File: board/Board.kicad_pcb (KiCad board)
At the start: 2 copper layers, 58.5 x 58.5 mm, 71 parts, among them J14 CONN_01X02, J15 CONN_01X07, J16 GS2, SW1 SW_Push, U1 STM32F410RBTx, U2 SN74LVC1G04, U3 LF33ABDT-TR, U4 ICM-20689, U5 MAG3110, U6 MS5637, Y1 25 MHz

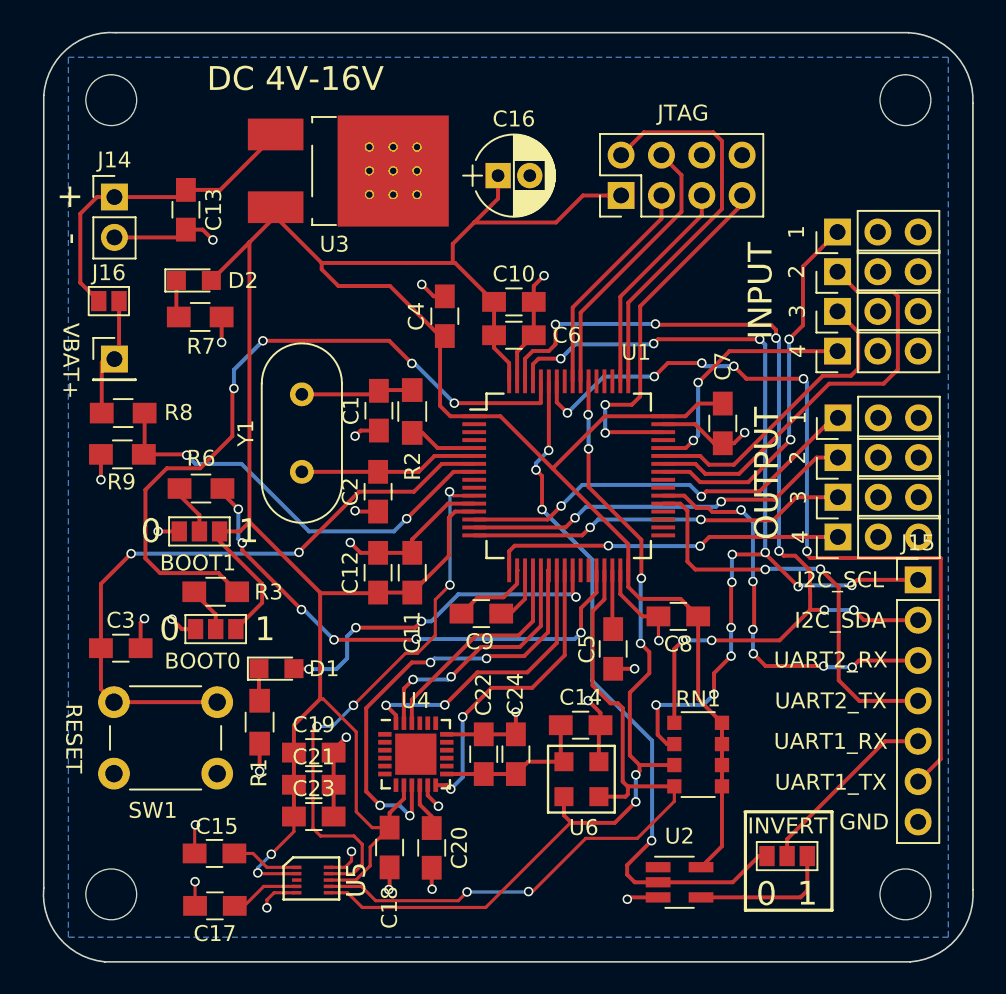
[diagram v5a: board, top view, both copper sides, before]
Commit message: fixed a few unconnected pads
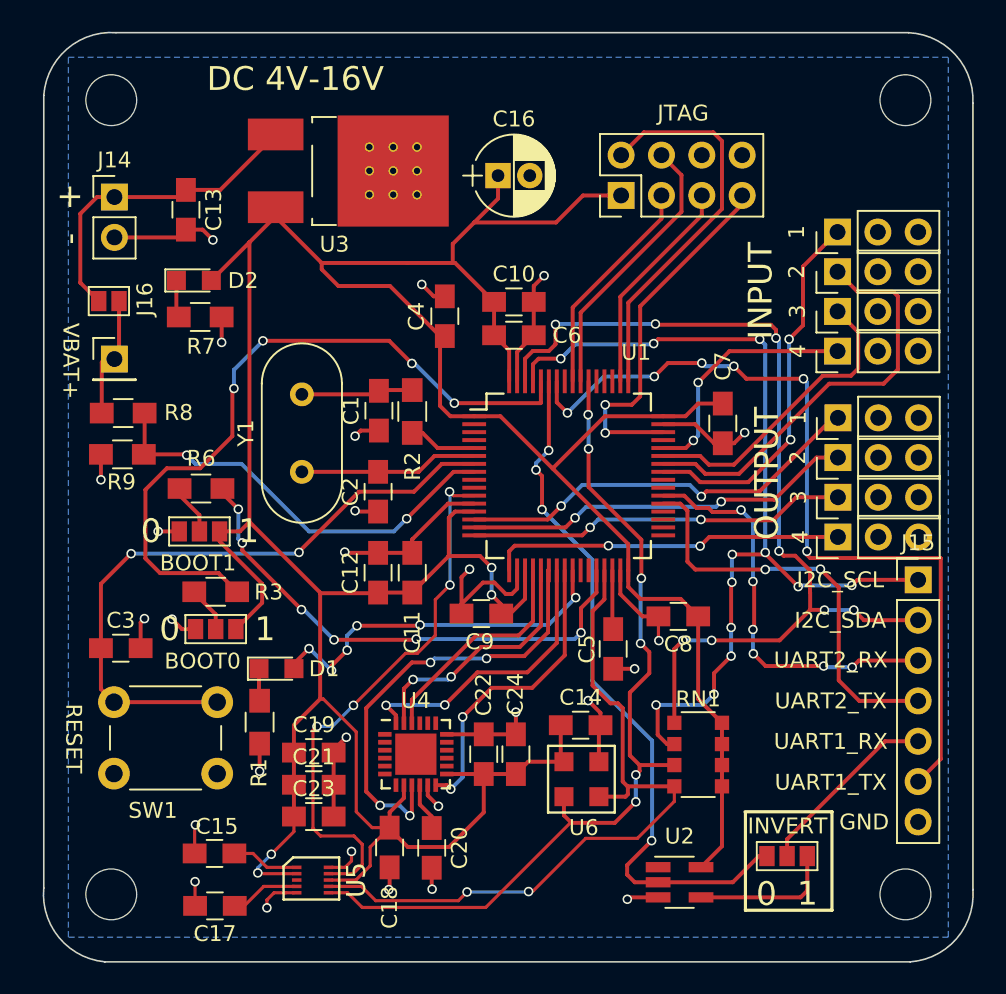
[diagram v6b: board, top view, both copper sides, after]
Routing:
- net VCC: track 216.6 -> 232.7 mm, vias 2 -> 4
- net GND: track 87.8 -> 92.0 mm, vias 26 -> 27
- net Net-(D1-Pad2): track 22.4 -> 23.5 mm, vias 4 -> 6

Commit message: more silkscreen
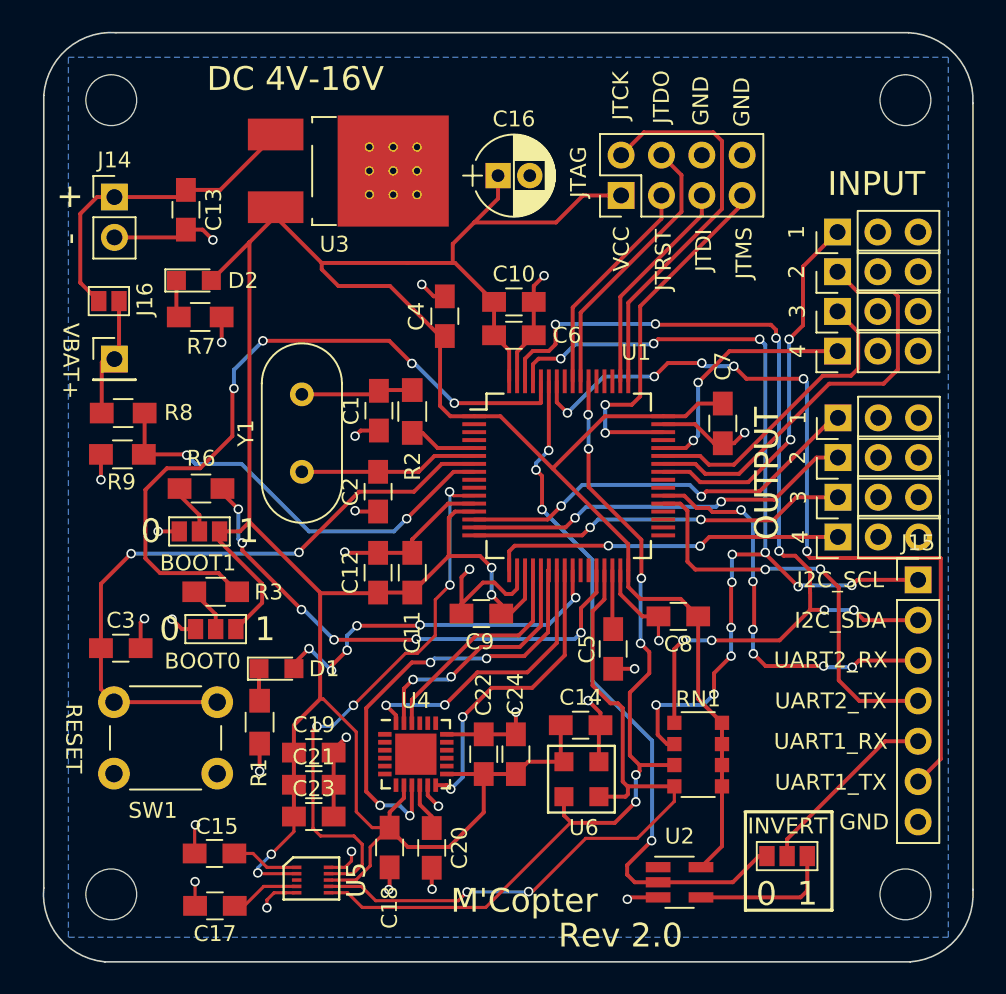
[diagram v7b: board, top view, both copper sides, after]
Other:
- board text added: "JTCK"
- board text added: "JTDI"
- board text added: "JTDO"
- board text added: "JTMS"
- board text added: "JTRST"
- board text added: "M'Copter"
- board text added: "Rev 2.0"
- board text added: "VCC"
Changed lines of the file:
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@@
     (links 161)
     (no_connects 0)
-    (area 90.442857 64.575 159.557143 125.275)
+    (area 95.681217 65.689424 154.310576 124.300001)
     (thickness 1.6)
-    (drawings 35)
+    (drawings 45)
     (tracks 790)
     (zones 0)
@@
   (page A4)
   (layers
-    (0 F.Cu signal)
-    (31 B.Cu signal)
+    (0 F.Cu signal hide)
+    (31 B.Cu signal hide)
     (32 B.Adhes user)
     (33 F.Adhes user)
@@
     (descr "Through hole straight pin header, 2x04, 2.54mm pitch, double rows")
     (tags "Through hole pin header THT 2x04 2.54mm double row")
-    (fp_text reference JTAG (at 5.18 3.9 180) (layer F.SilkS)
+    (fp_text reference JTAG (at 1.47 -2.68 90) (layer F.SilkS)
       (effects (font (size 1 1) (thickness 0.15)))
     )
@@
     (fp_line (start 4.35 9.4) (end 4.35 -1.8) (layer F.CrtYd) (width 0.05))
     (fp_line (start 4.35 -1.8) (end -1.8 -1.8) (layer F.CrtYd) (width 0.05))
-    (fp_text user %R (at 5.19 3.9 180) (layer F.Fab)
+    (fp_text user %R (at 1.47 -2.68 270) (layer F.Fab)
       (effects (font (size 1 1) (thickness 0.15)))
     )
@@
     )
   )
+  (gr_text "Rev 2.0" (at 132.06 122.59) (layer F.SilkS)
+    (effects (font (size 1.5 1.5) (thickness 0.3)))
+  )
+  (gr_text M'Copter (at 126 120.4) (layer F.SilkS)
+    (effects (font (size 1.5 1.5) (thickness 0.3)))
+  )
+  (gr_text JTMS (at 139.84 79.63 90) (layer F.SilkS)
+    (effects (font (size 1 1) (thickness 0.2)))
+  )
+  (gr_text JTDI (at 137.3 79.45 90) (layer F.SilkS)
+    (effects (font (size 1 1) (thickness 0.2)))
+  )
+  (gr_text JTRST (at 134.76 80.06 90) (layer F.SilkS)
+    (effects (font (size 1 1) (thickness 0.2)))
+  )
+  (gr_text VCC (at 132.12 79.37 90) (layer F.SilkS)
+    (effects (font (size 1 1) (thickness 0.2)))
+  )
+  (gr_text GND (at 139.7 70.12 90) (layer F.SilkS)
+    (effects (font (size 1 1) (thickness 0.2)))
+  )
+  (gr_text GND (at 137.12 70.04 90) (layer F.SilkS)
+    (effects (font (size 1 1) (thickness 0.2)))
+  )
+  (gr_text JTDO (at 134.64 69.8 90) (layer F.SilkS)
+    (effects (font (size 1 1) (thickness 0.2)))
+  )
+  (gr_text JTCK (at 132.08 69.72 90) (layer F.SilkS)
+    (effects (font (size 1 1) (thickness 0.2)))
+  )
   (gr_text BOOT1 (at 105.46 99.14) (layer F.SilkS)
     (effects (font (size 1 1) (thickness 0.2)))
@@
     (effects (font (size 1.5 1.5) (thickness 0.3)))
   )
-  (gr_text INPUT (at 140.875 82 90) (layer F.SilkS)
+  (gr_text INPUT (at 148.17 75.27) (layer F.SilkS)
     (effects (font (size 1.5 1.5) (thickness 0.3)))
   )
@@
     (min_thickness 0.254)
     (keepout (tracks not_allowed) (vias not_allowed) (copperpour not_allowed))
-    (fill yes (arc_segments 16) (thermal_gap 0.508) (thermal_bridge_width 0.508))
+    (fill (arc_segments 16) (thermal_gap 0.508) (thermal_bridge_width 0.508))
     (polygon
       (pts
